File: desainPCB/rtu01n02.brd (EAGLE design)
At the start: 74.9 x 70.8 mm, 12 parts, among them M1 ARDUINO-PRO-MINI-5.0V, U1 GY-521MPU6050, X1 JST-XH-02-PIN-LONG-PAD

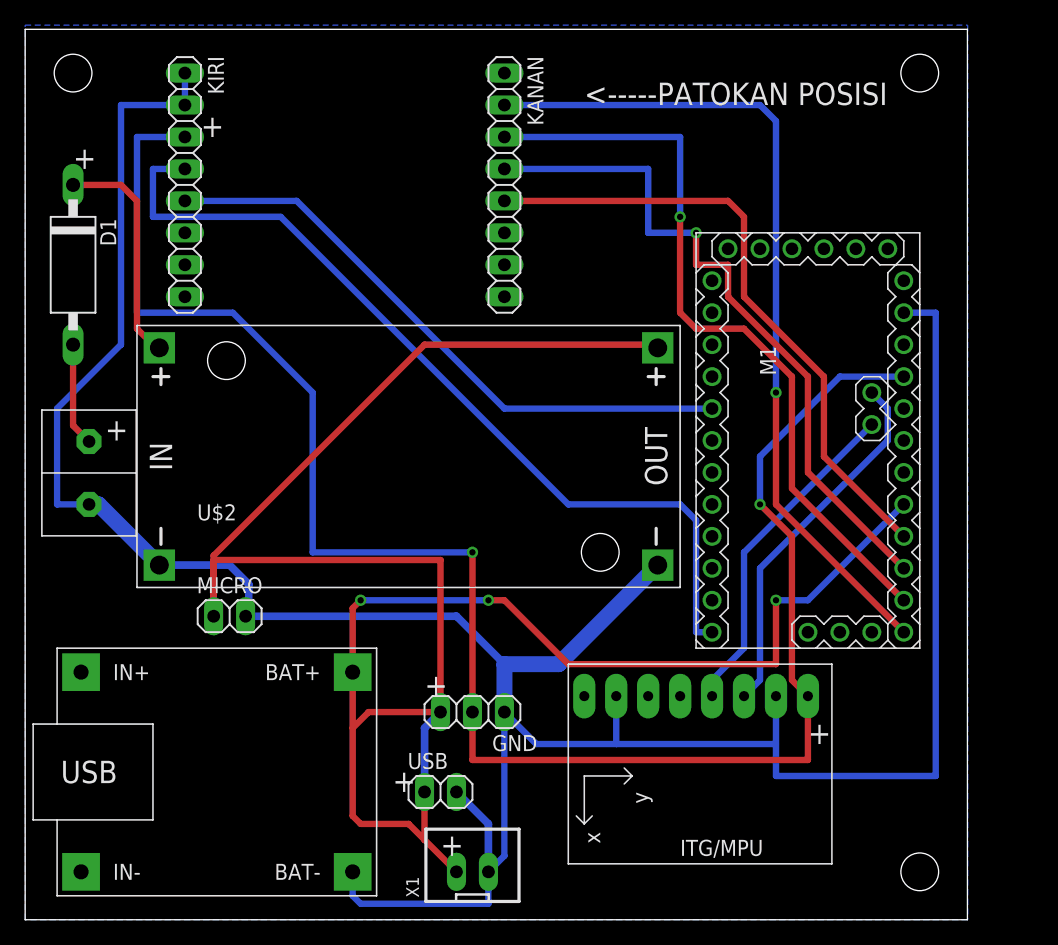
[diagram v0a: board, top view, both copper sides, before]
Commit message: new sensor suhu
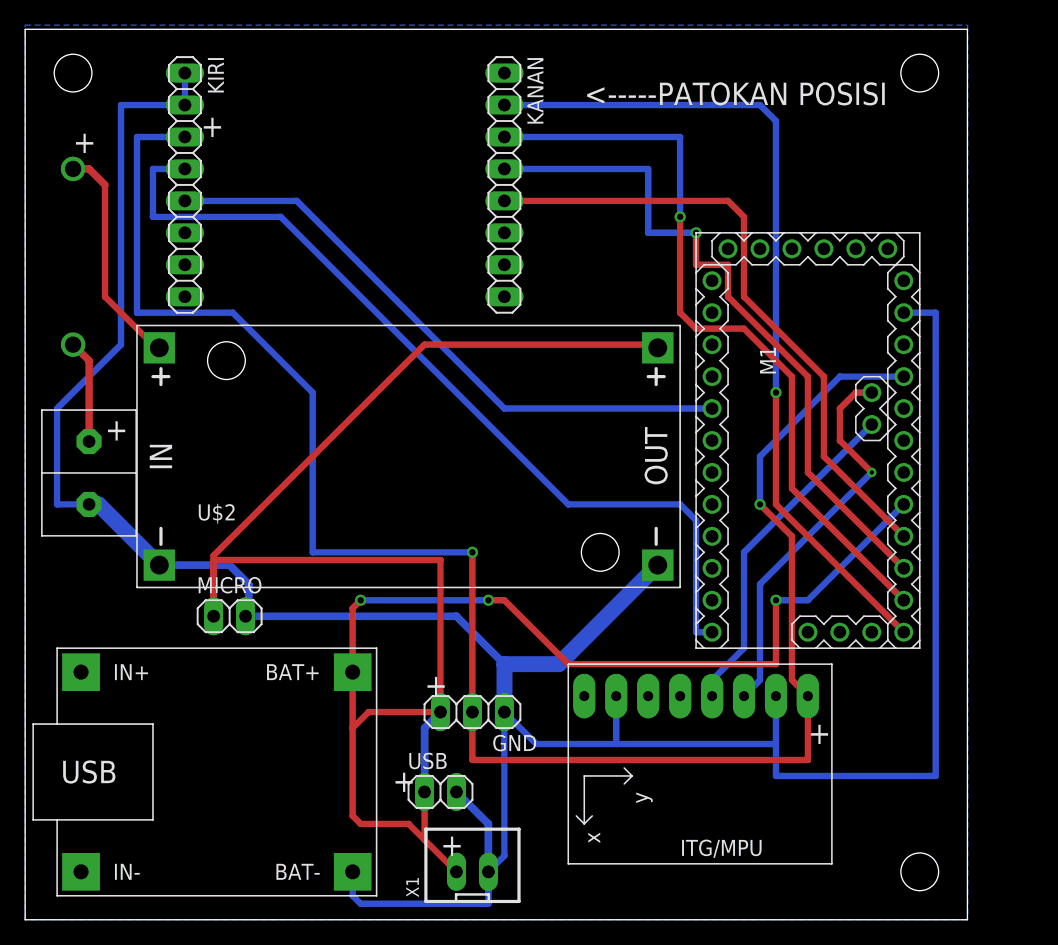
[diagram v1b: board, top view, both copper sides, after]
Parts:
- removed D1: 1N5060GP, diode:DO15-12
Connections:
- removed net N$1: D1.A, U$1.P1
- removed net N$2: 12V-5V1.IN+, D1.C
- new net IN+: U$1.P1
- new net OUT+: 12V-5V1.IN+
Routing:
- net N$2: track 18.2 -> 0.00 mm
- net OUT+: track 0.00 -> 18.0 mm, vias 0 -> 1
- net N$1: track 8.23 -> 0.00 mm
- net IN+: track 0.00 -> 8.23 mm, vias 0 -> 1
- net A5: track 29.4 -> 31.2 mm, vias 0 -> 1
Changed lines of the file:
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@@
 <dimension x1="26.035" y1="19.685" x2="26.035" y2="3.81" x3="27.94" y3="11.7475" textsize="1.778" layer="21"/>
 <text x="6.35" y="38.1" size="1.778" layer="21">+</text>
-<text x="3.81" y="59.69" size="1.778" layer="21">+</text>
+<text x="3.81" y="60.96" size="1.778" layer="21">+</text>
 <text x="13.97" y="62.23" size="1.778" layer="21">+</text>
 <text x="29.21" y="10.16" size="1.778" layer="21">+</text>
@@
 <attribute name="VALUE" x="30.48" y="6.985" size="1.27" layer="27"/>
 </element>
-<element name="D1" library="diode" library_urn="urn:adsk.eagle:library:210" package="DO15-12" package3d_urn="urn:adsk.eagle:package:43369/2" value="1N5060GP" x="3.81" y="52.07" smashed="yes" rot="R270">
-<attribute name="NAME" x="5.969" y="55.753" size="1.27" layer="25" ratio="10" rot="R270"/>
-<attribute name="POPULARITY" value="0" x="3.81" y="52.07" size="1.778" layer="27" rot="R270" display="off"/>
-<attribute name="VALUE" x="2.413" y="54.229" size="1.27" layer="27" ratio="10" rot="R270"/>
-</element>
 </elements>
 <signals>
@@
 <contactref element="M1" pad="J2.2"/>
 <contactref element="U1" pad="SCL"/>
-<wire x1="67.31" y1="41.91" x2="68.58" y2="40.64" width="0.508" layer="16"/>
-<wire x1="68.58" y1="38.1" x2="58.42" y2="27.94" width="0.508" layer="16"/>
-<wire x1="58.42" y1="27.94" x2="58.42" y2="19.05" width="0.508" layer="16"/>
+<wire x1="58.42" y1="26.67" x2="58.42" y2="19.05" width="0.508" layer="16"/>
 <wire x1="58.42" y1="19.05" x2="57.15" y2="17.78" width="0.508" layer="16"/>
-<wire x1="68.58" y1="40.64" x2="68.58" y2="38.1" width="0.508" layer="16"/>
+<wire x1="58.42" y1="26.67" x2="67.31" y2="35.56" width="0.508" layer="16"/>
+<via x="67.31" y="35.56" extent="1-16" drill="0.35"/>
+<wire x1="67.31" y1="35.56" x2="64.77" y2="38.1" width="0.508" layer="1"/>
+<wire x1="64.77" y1="38.1" x2="64.77" y2="40.64" width="0.508" layer="1"/>
+<wire x1="64.77" y1="40.64" x2="66.04" y2="41.91" width="0.508" layer="1"/>
+<wire x1="66.04" y1="41.91" x2="67.31" y2="41.91" width="0.508" layer="1"/>
 </signal>
 <signal name="2">
@@
 <wire x1="58.42" y1="64.77" x2="38.1" y2="64.77" width="0.508" layer="16"/>
 </signal>
-<signal name="N$1">
+<signal name="OUT+">
+<contactref element="12V-5V1" pad="IN+"/>
+<wire x1="6.35" y1="58.42" x2="6.35" y2="49.53" width="0.508" layer="1"/>
+<wire x1="6.35" y1="49.53" x2="10.414" y2="45.466" width="0.508" layer="1"/>
+<wire x1="10.414" y1="45.466" x2="10.668" y2="45.466" width="0.508" layer="1"/>
+<via x="3.81" y="59.69" extent="1-16" drill="1.3" shape="square"/>
+<wire x1="3.81" y1="59.69" x2="5.08" y2="59.69" width="0.59" layer="1"/>
+<wire x1="5.08" y1="59.69" x2="6.35" y2="58.42" width="0.59" layer="1"/>
+</signal>
+<signal name="IN+">
 <contactref element="U$1" pad="P1"/>
-<contactref element="D1" pad="A"/>
-<wire x1="5.08" y1="38.02" x2="3.81" y2="39.29" width="0.508" layer="1"/>
-<wire x1="3.81" y1="39.29" x2="3.81" y2="45.72" width="0.508" layer="1"/>
-</signal>
-<signal name="N$2">
-<contactref element="D1" pad="C"/>
-<contactref element="12V-5V1" pad="IN+"/>
-<wire x1="3.81" y1="58.42" x2="7.62" y2="58.42" width="0.508" layer="1"/>
-<wire x1="7.62" y1="58.42" x2="8.89" y2="57.15" width="0.508" layer="1"/>
-<wire x1="8.89" y1="57.15" x2="8.89" y2="46.99" width="0.508" layer="1"/>
-<wire x1="8.89" y1="46.99" x2="10.414" y2="45.466" width="0.508" layer="1"/>
-<wire x1="10.414" y1="45.466" x2="10.668" y2="45.466" width="0.508" layer="1"/>
+<via x="3.81" y="45.72" extent="1-16" drill="1.3" shape="square"/>
+<wire x1="3.81" y1="45.72" x2="5.08" y2="44.45" width="0.59" layer="1"/>
+<wire x1="5.08" y1="44.45" x2="5.08" y2="38.02" width="0.59" layer="1"/>
 </signal>
 </signals>
